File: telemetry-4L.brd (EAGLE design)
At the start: 69.8 x 22.9 mm, 72 parts, among them SW1 MF-SW-TACT-4.2MM, SW2 PCM12SMTR, U1 ATSAMD21G18A-MUT, U2 SPX3819M5-L-3-0, U3 MCP73831T-2ACI/OT, U4 IRLML6344TRPBF, U5 SIM868, U6 BMP280, U7 MPU-9250, U8 TPS61253YFFR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

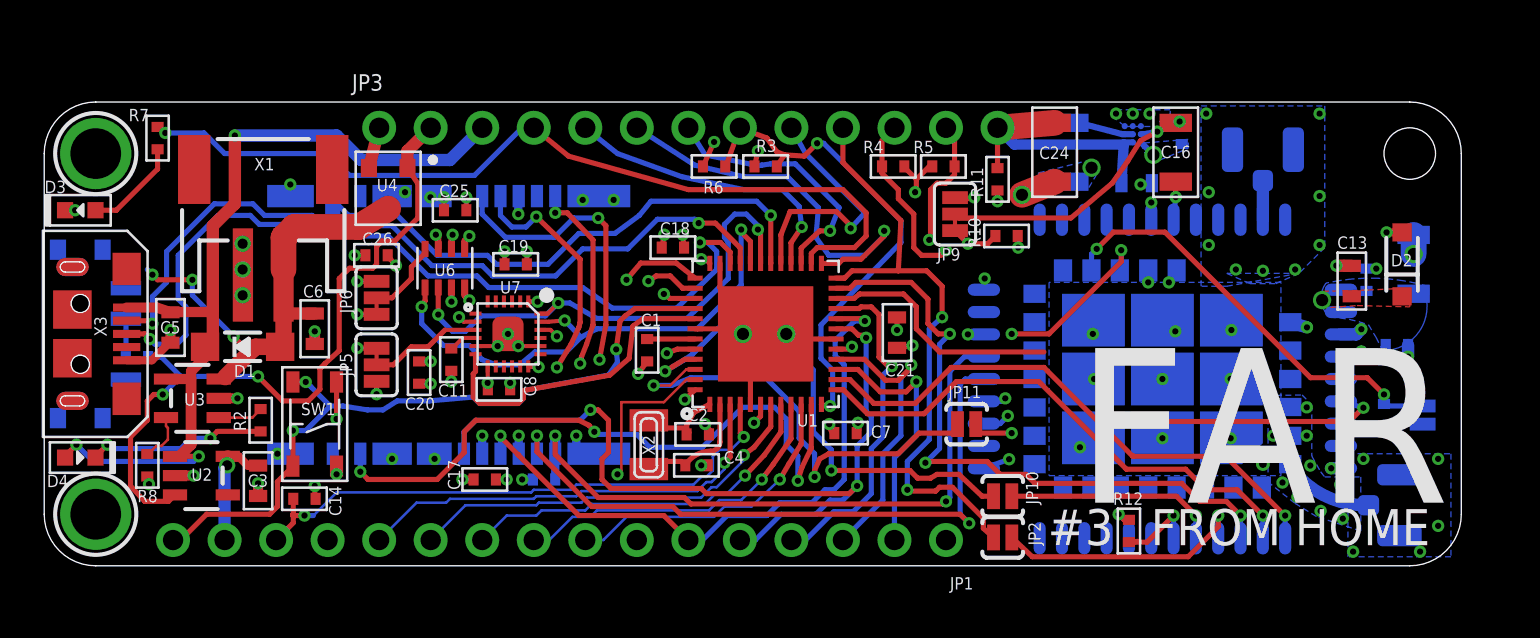
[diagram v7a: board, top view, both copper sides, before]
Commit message: fixed more margins Remember: Have a look at A5 trace and via
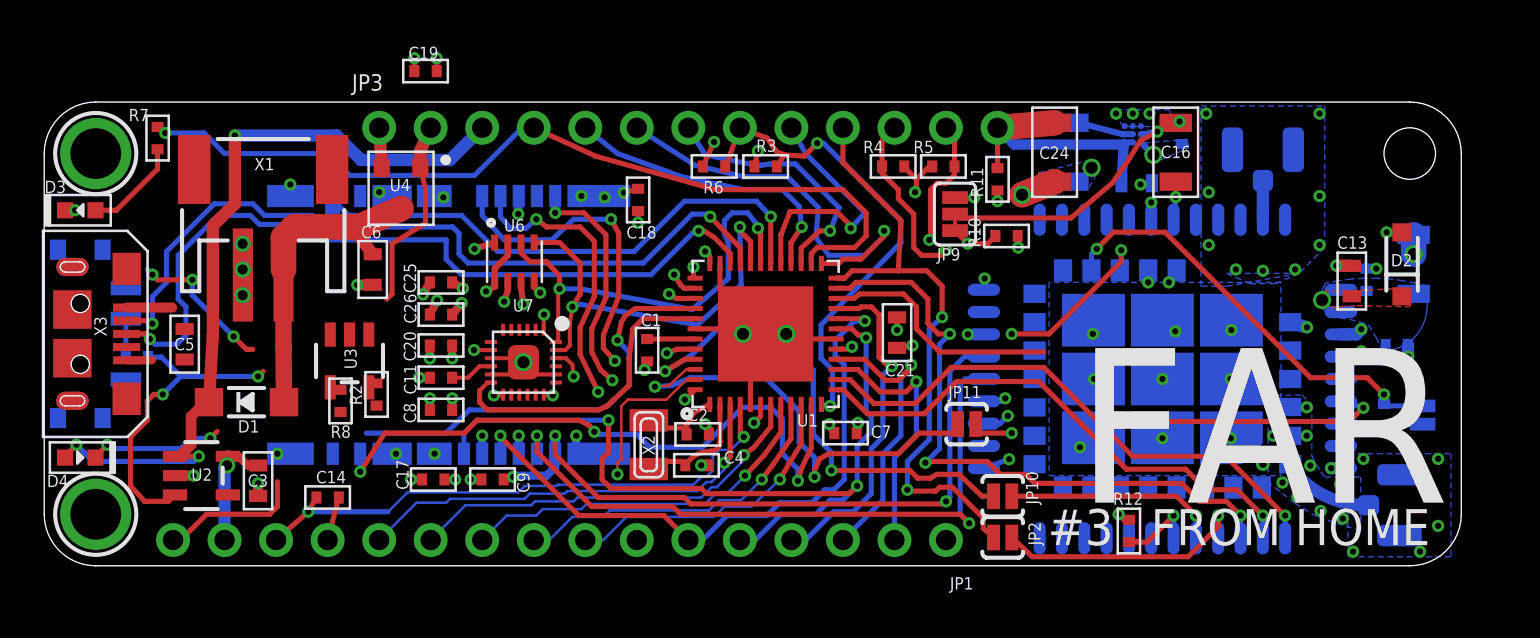
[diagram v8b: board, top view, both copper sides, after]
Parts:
- removed JP5, JP6: JUMPER-PAD-3-2OF3_NC_BY_TRACE_SMALL, SparkFun-Passives:PAD-JUMPER-3-2OF3_NC_BY_TRACE_YES_SILK_FULL_BOX
- removed SW1: MF-SW-TACT-4.2MM, MF_Switches:TACT4.2MM
- moved C19 10.5 mm to (18.8, 24.4)
- moved R8 10.0 mm to (14.6, 8.13)
- moved U3 7.96 mm to (15.0, 10.1), turned to 180 degrees
- moved R2 5.85 mm to (16.4, 8.45)
- moved C26 4.31 mm to (19.6, 12.4)
- moved C6 4.09 mm to (16.2, 14.6)
- moved C25 3.62 mm to (19.6, 14.0)
- moved U6 3.44 mm to (23.2, 15.0), turned to 90 degrees
- moved C8 3.03 mm to (19.6, 7.68), turned to 0 degrees
- moved C18 2.91 mm to (29.3, 18.0), turned to 90 degrees
- moved D1 2.74 mm to (9.97, 8.06)
- moved C9 2.54 mm to (22.1, 4.25), flipped to the top, turned to 180 degrees
- moved C17 2.54 mm to (19.2, 4.25)
- moved C20 1.72 mm to (19.6, 10.9), turned to 0 degrees
- moved U7 1.59 mm to (23.6, 10.0)
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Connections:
- removed net N$10: JP6.2, U6.P5
- removed net N$2: JP5.2, U7.9
- net !RESET: no longer SW1.P$1, SW1.P$2
- net +3V: no longer JP5.1, JP6.1
- net GND: now also U6.P5, U7.9; no longer JP5.3, JP6.3, SW1.P$3, SW1.P$4
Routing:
- net EN: track 35.7 -> 25.3 mm
- net !RESET: track 35.9 -> 28.2 mm, vias 3 -> 1
- net N$2: track 5.59 -> 0.00 mm
- net SCL: track 46.0 -> 41.0 mm, vias 4 -> 3
- net N$10: track 3.85 -> 0.00 mm
- net SDA: track 40.3 -> 37.1 mm, vias 4 -> 3
- net D+: track 41.5 -> 39.0 mm
- net N$4: track 2.42 -> 0.00 mm
- net VBUS: track 45.0 -> 42.6 mm
- net N$3: track 2.24 -> 0.00 mm
- net SIM_VDD: track 31.9 -> 34.1 mm, vias 2 -> 3
- net N$1: track 8.86 -> 6.72 mm
- net +3V: track 80.8 -> 82.7 mm, vias 24 -> 22
- net TX5/GPS_RX: track 35.0 -> 33.7 mm
- net GND: track 77.3 -> 76.3 mm, vias 105 -> 96
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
